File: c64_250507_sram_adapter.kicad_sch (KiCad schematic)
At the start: 19 parts, among them J1 TL_DRAM, J10 B_03, J2 TR_DRAM, J3 BL_DRAM, J4 BR_DRAM, J5 T_01, J6 T_02, J7 T_03, J8 B_01, J9 B_02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

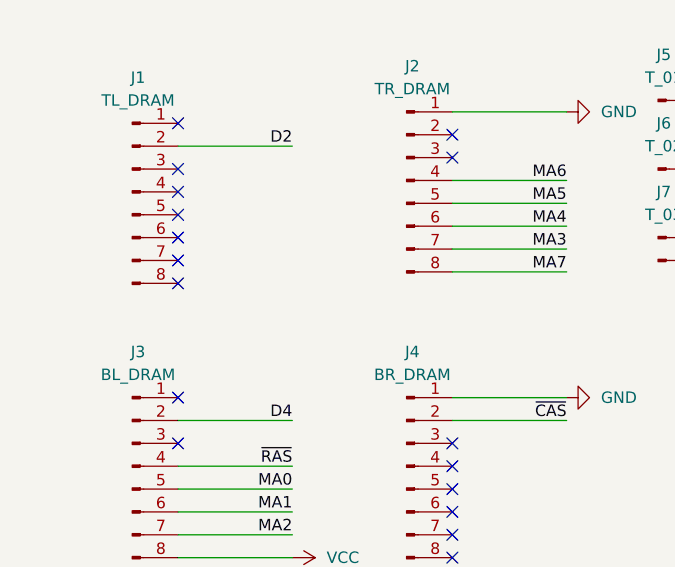
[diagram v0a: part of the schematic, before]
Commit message: Rev. 1 with better power trace
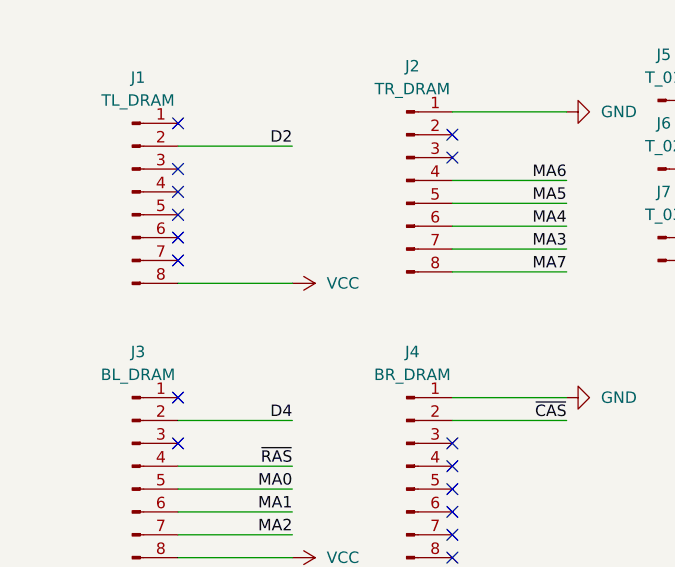
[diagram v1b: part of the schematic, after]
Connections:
- net VCC: now also J1.8 (Pin_8)
- no-connect marks 23 -> 22
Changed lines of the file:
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@@
 	)
 	(no_connect
-		(at 35.56 45.72)
-	)
-	(no_connect
 		(at 35.56 33.02)
 	)
@@
 	(wire
 		(pts
+			(xy 35.56 45.72) (xy 48.26 45.72)
+		)
+		(stroke
+			(width 0)
+			(type default)
+		)
+	)
+	(wire
+		(pts
 			(xy 114.3 158.75) (xy 120.65 158.75)
 		)
@@
 		(on_board yes)
 		(dnp no)
-		(fields_autoplaced yes)
 		(property "Reference" "#PWR02"
 			(at 44.45 76.2 0)
@@
 				)
 			)
+		)
+	)
+	(symbol
+		(lib_id "power:VCC")
+		(at 48.26 45.72 270)
+		(unit 1)
+		(exclude_from_sim no)
+		(in_bom yes)
+		(on_board yes)
+		(dnp no)
+		(property "Reference" "#PWR030"
+			(at 44.45 45.72 0)
+			(effects
+				(font
+					(size 1.27 1.27)
+				)
+				(hide yes)
+			)
+		)
+		(property "Value" "VCC"
+			(at 52.07 45.7199 90)
+			(effects
+				(font
+					(size 1.27 1.27)
+				)
+				(justify left)
+			)
+		)
+		(property "Footprint" ""
+			(at 48.26 45.72 0)
+			(effects
+				(font
+					(size 1.27 1.27)
+				)
+				(hide yes)
+			)
+		)
+		(property "Datasheet" ""
+			(at 48.26 45.72 0)
+			(effects
+				(font
+					(size 1.27 1.27)
+				)
+				(hide yes)
+			)
+		)
+		(property "Description" "Power symbol creates a global label with name \"VCC\""
+			(at 48.26 45.72 0)
+			(effects
+				(font
+					(size 1.27 1.27)
+				)
+				(hide yes)
+			)
+		)
+		(pin "1"
+		)
+		(instances
+			(project "c64_250507_sram_adapter"
+				(path "/b7cf27c3-6e64-434e-9e75-1cebfe3724bd"
+					(reference "#PWR030")
+					(unit 1)
+				)
+			)
